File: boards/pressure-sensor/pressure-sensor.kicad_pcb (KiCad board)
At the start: 2 copper layers, 26.7 x 24.1 mm, 4 parts, among them J1 CONN_01X04_MALE, M3 MountingHole_3.2mm_M3

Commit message: boards/pressure-sensor: added 3d-Model and labels
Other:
- board text added: "rexus-viper pressure sensor ©rchojetzki"
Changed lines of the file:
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@@
     (area 143.434999 100.254999 170.255001 124.535001)
     (thickness 1.6)
-    (drawings 6)
+    (drawings 7)
     (tracks 27)
     (zones 0)
@@
     (pad_to_mask_clearance 0.2)
     (aux_axis_origin 0 0)
-    (visible_elements FFFFFF7F)
+    (visible_elements 7FFFFFFF)
     (pcbplotparams
       (layerselection 0x00030_80000001)
@@
       (rotate (xyz 0 0 90))
     )
+  )
+  (module Mounting_Holes:MountingHole_3.2mm_M3 (layer F.Cu)
+    (at 148.59 119.38)
+    (descr "Mounting Hole 3.2mm, no annular, M3")
+    (tags "mounting hole 3.2mm no annular m3")
+    (fp_text reference M3 (at 0 3.81) (layer F.SilkS)
+      (effects (font (size 1 1) (thickness 0.15)))
+    )
+    (fp_text value MountingHole_3.2mm_M3 (at 0 4.2) (layer F.Fab)
+      (effects (font (size 1 1) (thickness 0.15)))
+    )
+    (fp_circle (center 0 0) (end 3.2 0) (layer Cmts.User) (width 0.15))
+    (fp_circle (center 0 0) (end 3.45 0) (layer F.CrtYd) (width 0.05))
+    (pad 1 np_thru_hole circle (at 0 0) (size 3.2 3.2) (drill 3.2) (layers *.Cu *.Mask))
+  )
+  (module Mounting_Holes:MountingHole_3.2mm_M3 (layer F.Cu)
+    (at 165.1 105.41)
+    (descr "Mounting Hole 3.2mm, no annular, M3")
+    (tags "mounting hole 3.2mm no annular m3")
+    (fp_text reference M3 (at 0 -4.2) (layer F.SilkS)
+      (effects (font (size 1 1) (thickness 0.15)))
+    )
+    (fp_text value MountingHole_3.2mm_M3 (at 0 4.2) (layer F.Fab)
+      (effects (font (size 1 1) (thickness 0.15)))
+    )
+    (fp_circle (center 0 0) (end 3.2 0) (layer Cmts.User) (width 0.15))
+    (fp_circle (center 0 0) (end 3.45 0) (layer F.CrtYd) (width 0.05))
+    (pad 1 np_thru_hole circle (at 0 0) (size 3.2 3.2) (drill 3.2) (layers *.Cu *.Mask))
   )
   (module rchojetzki-pressure-sensor-board:AMS_5915-XXXX-D_differential_pressure_sensor (layer F.Cu)
@@
     (pad 8 thru_hole circle (at 3.81 -15.24 270) (size 1.524 1.524) (drill 0.762) (layers *.Cu *.Mask)
       (net 8 "Net-(PS1-Pad8)"))
-  )
-  (module Mounting_Holes:MountingHole_3.2mm_M3 (layer F.Cu)
-    (at 148.59 119.38)
-    (descr "Mounting Hole 3.2mm, no annular, M3")
-    (tags "mounting hole 3.2mm no annular m3")
-    (fp_text reference M3 (at 0 3.81) (layer F.SilkS)
-      (effects (font (size 1 1) (thickness 0.15)))
-    )
-    (fp_text value MountingHole_3.2mm_M3 (at 0 4.2) (layer F.Fab)
-      (effects (font (size 1 1) (thickness 0.15)))
-    )
-    (fp_circle (center 0 0) (end 3.2 0) (layer Cmts.User) (width 0.15))
-    (fp_circle (center 0 0) (end 3.45 0) (layer F.CrtYd) (width 0.05))
-    (pad 1 np_thru_hole circle (at 0 0) (size 3.2 3.2) (drill 3.2) (layers *.Cu *.Mask))
-  )
-  (module Mounting_Holes:MountingHole_3.2mm_M3 (layer F.Cu)
-    (at 165.1 105.41)
-    (descr "Mounting Hole 3.2mm, no annular, M3")
-    (tags "mounting hole 3.2mm no annular m3")
-    (fp_text reference M3 (at 0 -4.2) (layer F.SilkS)
-      (effects (font (size 1 1) (thickness 0.15)))
-    )
-    (fp_text value MountingHole_3.2mm_M3 (at 0 4.2) (layer F.Fab)
-      (effects (font (size 1 1) (thickness 0.15)))
-    )
-    (fp_circle (center 0 0) (end 3.2 0) (layer Cmts.User) (width 0.15))
-    (fp_circle (center 0 0) (end 3.45 0) (layer F.CrtYd) (width 0.05))
-    (pad 1 np_thru_hole circle (at 0 0) (size 3.2 3.2) (drill 3.2) (layers *.Cu *.Mask))
+    (model F:/Richard/dev/viper/elektronik_repo/rexus-viper-elektronik/boards/pressure-sensor/rchojetzki-pressure-sensor-board.pretty/AMS_5915-XXXX-D_differential_pressure_sensor.wrl
+      (at (xyz 0 0 0))
+      (scale (xyz 1 1 1))
+      (rotate (xyz 0 0 0))
+    )
+  )
+  (gr_text "rexus-viper\npressure sensor\n©rchojetzki" (at 159.004 114.554 90) (layer B.SilkS)
+    (effects (font (size 1.5 1.5) (thickness 0.3)) (justify mirror))
   )
   (gr_line (start 170.18 124.46) (end 148.59 124.46) (angle 90) (layer Edge.Cuts) (width 0.15))
@@
   (gr_line (start 143.51 124.46) (end 148.59 124.46) (angle 90) (layer Edge.Cuts) (width 0.15))
   (gr_line (start 143.51 119.38) (end 143.51 124.46) (angle 90) (layer Edge.Cuts) (width 0.15))
-  (segment (start 153.67 115.57) (end 154.94 115.57) (width 0.6) (layer F.Cu) (net 1) (status 400000))
-  (segment (start 155.8036 105.0036) (end 148.5011 105.0036) (width 0.6) (layer F.Cu) (net 1) (status 800000))
+  (segment (start 153.67 115.57) (end 154.94 115.57) (width 0.6) (layer F.Cu) (net 1))
+  (segment (start 155.8036 105.0036) (end 148.5011 105.0036) (width 0.6) (layer F.Cu) (net 1))
   (segment (start 156.21 105.41) (end 155.8036 105.0036) (width 0.6) (layer F.Cu) (net 1))
   (segment (start 156.21 114.3) (end 156.21 105.41) (width 0.6) (layer F.Cu) (net 1))
   (segment (start 154.94 115.57) (end 156.21 114.3) (width 0.6) (layer F.Cu) (net 1))
-  (segment (start 153.67 113.03) (end 153.67 107.95) (width 0.6) (layer F.Cu) (net 2) (status 400000))
-  (segment (start 153.2636 107.5436) (end 148.5011 107.5436) (width 0.6) (layer F.Cu) (net 2) (status 800000))
+  (segment (start 153.67 113.03) (end 153.67 107.95) (width 0.6) (layer F.Cu) (net 2))
+  (segment (start 153.2636 107.5436) (end 148.5011 107.5436) (width 0.6) (layer F.Cu) (net 2))
   (segment (start 153.67 107.95) (end 153.2636 107.5436) (width 0.6) (layer F.Cu) (net 2))
-  (segment (start 148.5011 107.5436) (end 148.9075 107.95) (width 0.6) (layer F.Cu) (net 2) (status C00000))
-  (segment (start 153.67 118.11) (end 154.94 118.11) (width 0.6) (layer F.Cu) (net 3) (status 400000))
-  (segment (start 150.2664 110.0836) (end 148.5011 110.0836) (width 0.6) (layer F.Cu) (net 3) (status 800000))
+  (segment (start 148.5011 107.5436) (end 148.9075 107.95) (width 0.6) (layer F.Cu) (net 2))
+  (segment (start 153.67 118.11) (end 154.94 118.11) (width 0.6) (layer F.Cu) (net 3))
+  (segment (start 150.2664 110.0836) (end 148.5011 110.0836) (width 0.6) (layer F.Cu) (net 3))
   (segment (start 151.13 109.22) (end 150.2664 110.0836) (width 0.6) (layer F.Cu) (net 3))
   (via (at 151.13 109.22) (size 0.6) (drill 0.4) (layers F.Cu B.Cu) (net 3))
@@
   (segment (start 156.21 116.84) (end 158.75 114.3) (width 0.6) (layer F.Cu) (net 3))
   (segment (start 154.94 118.11) (end 156.21 116.84) (width 0.6) (layer F.Cu) (net 3))
-  (segment (start 153.67 120.65) (end 154.94 120.65) (width 0.6) (layer F.Cu) (net 4) (status 400000))
-  (segment (start 150.2664 112.6236) (end 148.5011 112.6236) (width 0.6) (layer F.Cu) (net 4) (status 800000))
+  (segment (start 153.67 120.65) (end 154.94 120.65) (width 0.6) (layer F.Cu) (net 4))
+  (segment (start 150.2664 112.6236) (end 148.5011 112.6236) (width 0.6) (layer F.Cu) (net 4))
   (segment (start 151.13 111.76) (end 150.2664 112.6236) (width 0.6) (layer F.Cu) (net 4))
   (via (at 151.13 111.76) (size 0.6) (drill 0.4) (layers F.Cu B.Cu) (net 4))

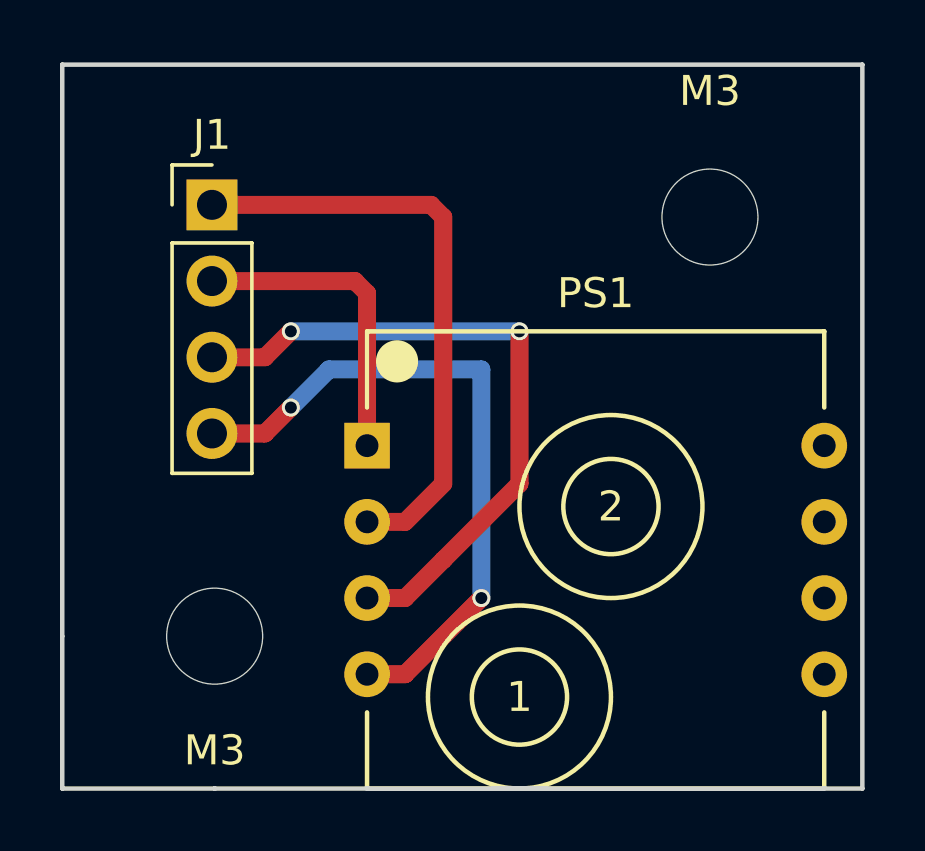
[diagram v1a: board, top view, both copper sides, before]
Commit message: boards/pressure_sensor: all complains addressed
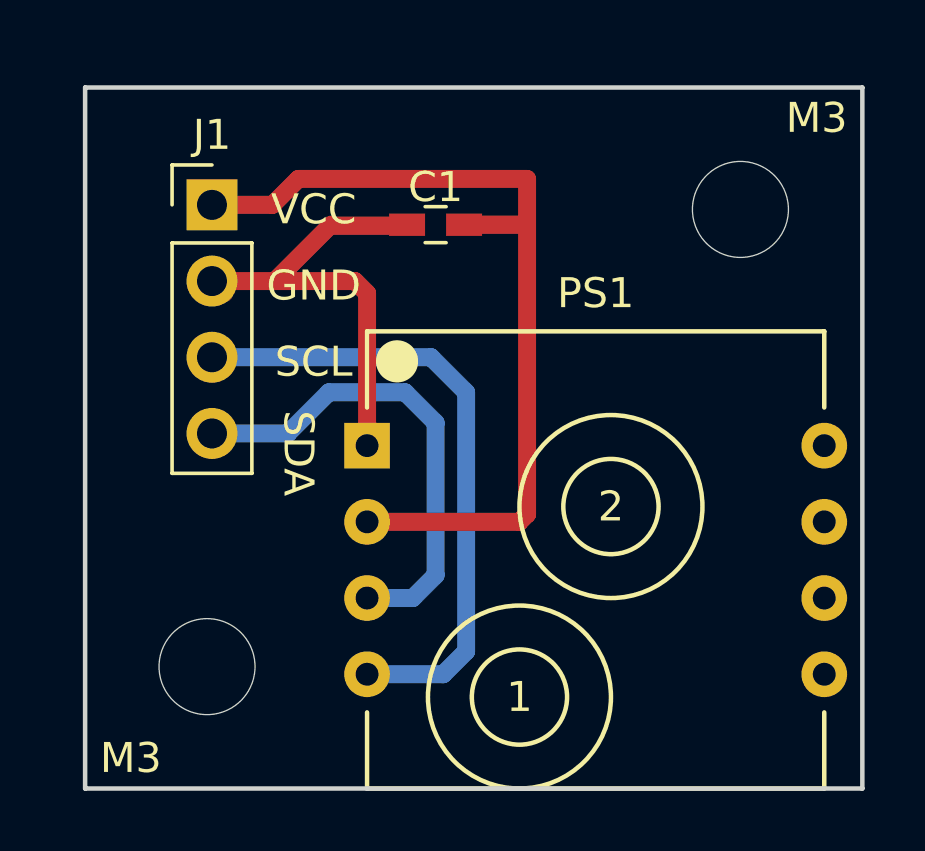
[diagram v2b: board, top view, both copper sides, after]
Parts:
- added C1: 100nf, Capacitors_SMD:C_0603_HandSoldering, F.Cu at (156.0, 105.7)
- moved M3 1.05 mm to (166.1, 105.2)
- moved M3 1.05 mm to (148.3, 120.4)
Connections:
- J1 pad 3: /SDA -> /SCL
- J1 pad 4: /SCL -> /SDA
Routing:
- net /VCC: track 19.8 -> 29.6 mm
- net /SDA: track 22.3 -> 16.1 mm, vias 2 -> 0
- net /GND: track 11.0 -> 16.2 mm
- net /SCL: track 22.3 -> 21.2 mm, vias 2 -> 0
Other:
- board size 26.7 x 24.1 mm -> 25.9 x 23.4 mm
- board text added: "GND"
- board text added: "SCL"
- board text added: "SDA"
- board text added: "VCC"

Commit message: [docs] export all board layouts
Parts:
- moved J1 110.1 mm to (63.4, 35.2)
- moved M3 110.1 mm to (81.0, 35.3)
- moved C1 110.1 mm to (70.9, 35.8)
- moved M3 110.1 mm to (63.2, 50.5)
- moved PS1 110.1 mm to (68.6, 39.4)
